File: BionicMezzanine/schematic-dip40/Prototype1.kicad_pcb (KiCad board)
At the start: 2 copper layers, 95.5 x 72 mm, 14 parts, among them J1 BionicConnector, J2 Conn_02x25_Odd_Even, J3 Conn_02x25_Odd_Even, J4 ZIF_Socket_40pin, J5 Conn_02x20_Odd_Even, J6 Conn_02x20_Odd_Even, J7 Conn_02x10_Odd_Even, J8 Conn_02x10_Odd_Even, U1 74HCT541

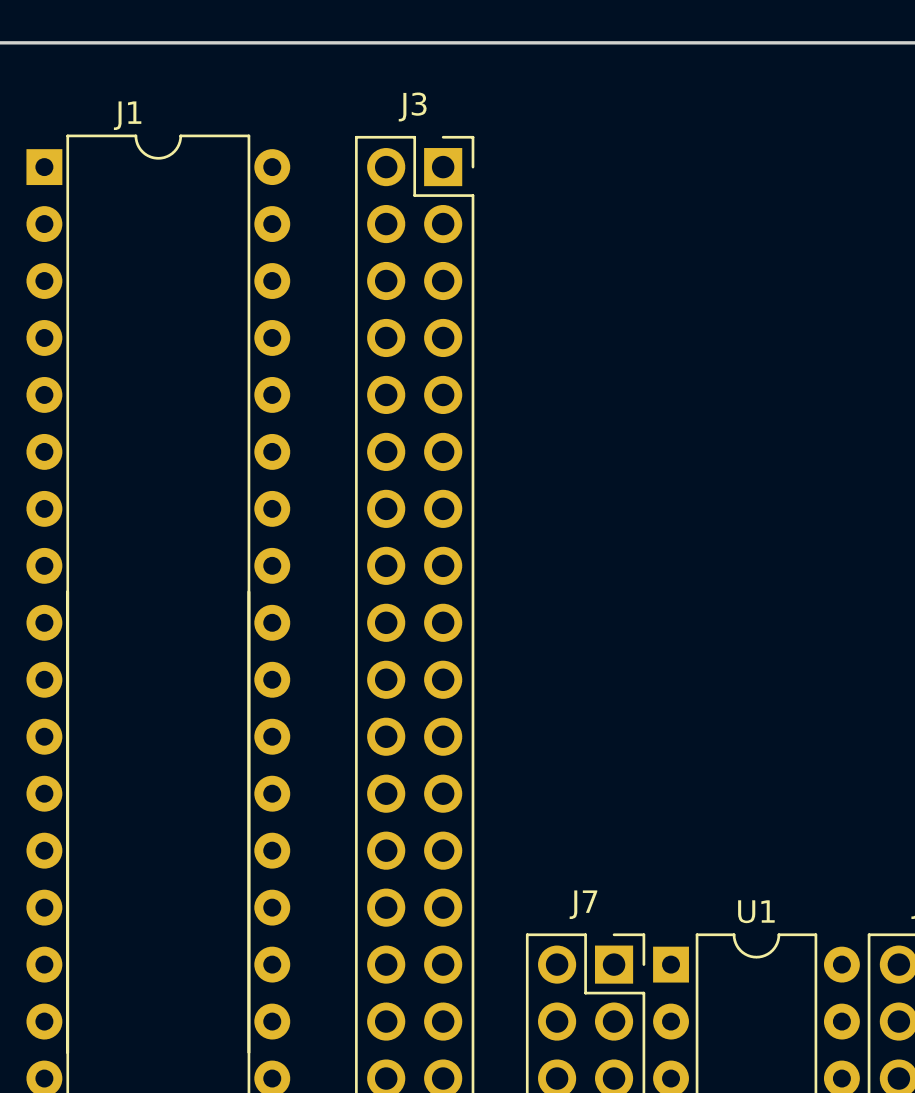
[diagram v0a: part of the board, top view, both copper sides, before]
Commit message: Migrate to KiCad 6.0
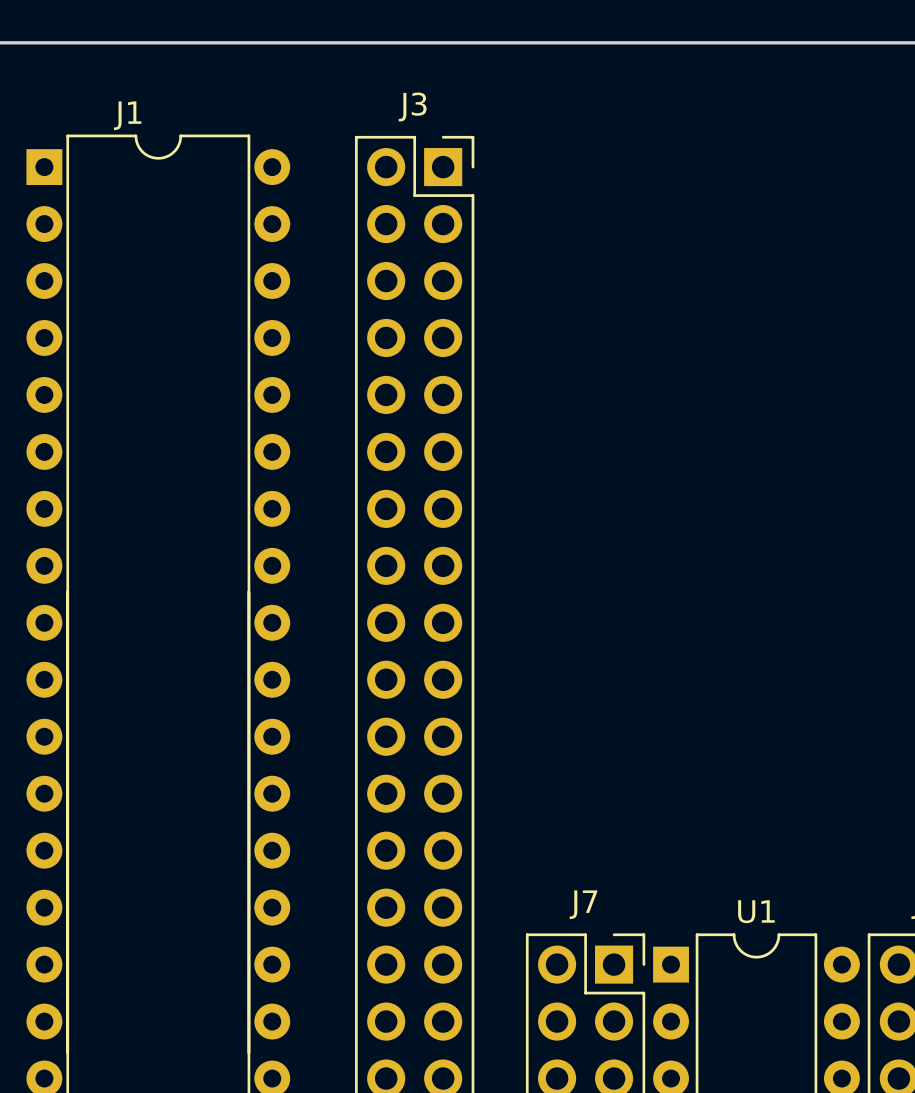
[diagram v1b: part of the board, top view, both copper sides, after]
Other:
- net class Default removed
